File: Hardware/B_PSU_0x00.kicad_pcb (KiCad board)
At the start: 2 copper layers, 111.8 x 73.7 mm, 103 parts, among them J1 Conn_01x03, J10 Conn_01x02, J11 Conn_01x02, J12 Conn_01x02, J13 Conn_01x02, J14 Conn_01x02, J15 Conn_01x02, J16 Conn_01x03, J17 Conn_01x02, J2 Conn_01x02, J3 Conn_01x02, J4 Conn_01x02, J5 Conn_01x02, J6 Conn_01x02, J7 Conn_01x03, J8 Conn_01x02, J9 Conn_01x03, U1 ADP5070AREZ, U2 ADP7142AUJZ, U3 ADP7182AUJZ, U5 ADP7142AUJZ, U7 ADP7182AUJZ, U8 ADP5070AREZ

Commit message: Update B_PSU_0x00.kicad_pcb
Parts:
- removed COUT3, COUT4: 10uF, Capacitor_SMD:C_1210_3225Metric_Pad1.33x2.70mm_HandSolder
- removed Cc3: 68nF, Capacitor_SMD:C_0805_2012Metric_Pad1.18x1.45mm_HandSolder
- removed Cc4: 47nF, Capacitor_SMD:C_0805_2012Metric_Pad1.18x1.45mm_HandSolder
- removed Cin2: 10uF, Capacitor_SMD:C_1206_3216Metric_Pad1.33x1.80mm_HandSolder
- removed Cvref2, Cvreg2: 1uF, Capacitor_SMD:C_0805_2012Metric_Pad1.18x1.45mm_HandSolder
- removed D10, D3: DFLS240, Diode_SMD:D_SOD-123F
- removed J11, J12, J17, J4, J6: Conn_01x02, Connector_PinHeader_2.54mm:PinHeader_1x02_P2.54mm_Vertical
- removed J15: Conn_01x02, TerminalBlock:TerminalBlock_bornier-2_P5.08mm
- removed J16: Conn_01x03, TerminalBlock:TerminalBlock_bornier-3_P5.08mm
- removed L3: 15uH, Inductor_SMD:L_Coilcraft_XxL4030
- removed L4: 6.8uH, Inductor_SMD:L_Coilcraft_XxL4040
- removed Rc3: 15k, Resistor_SMD:R_0805_2012Metric_Pad1.20x1.40mm_HandSolder
- removed Rc4: 12k, Resistor_SMD:R_0805_2012Metric_Pad1.20x1.40mm_HandSolder
- removed Rfb10, Rfb9: 113k, Resistor_SMD:R_0805_2012Metric_Pad1.20x1.40mm_HandSolder
- removed Rft10, Rft9: 2.15M, Resistor_SMD:R_0805_2012Metric_Pad1.20x1.40mm_HandSolder
- removed U8: ADP5070AREZ, Package_SO:ETSSOP-20-1EP_4.4x6.5mm_P0.65mm_EP3x4.2mm

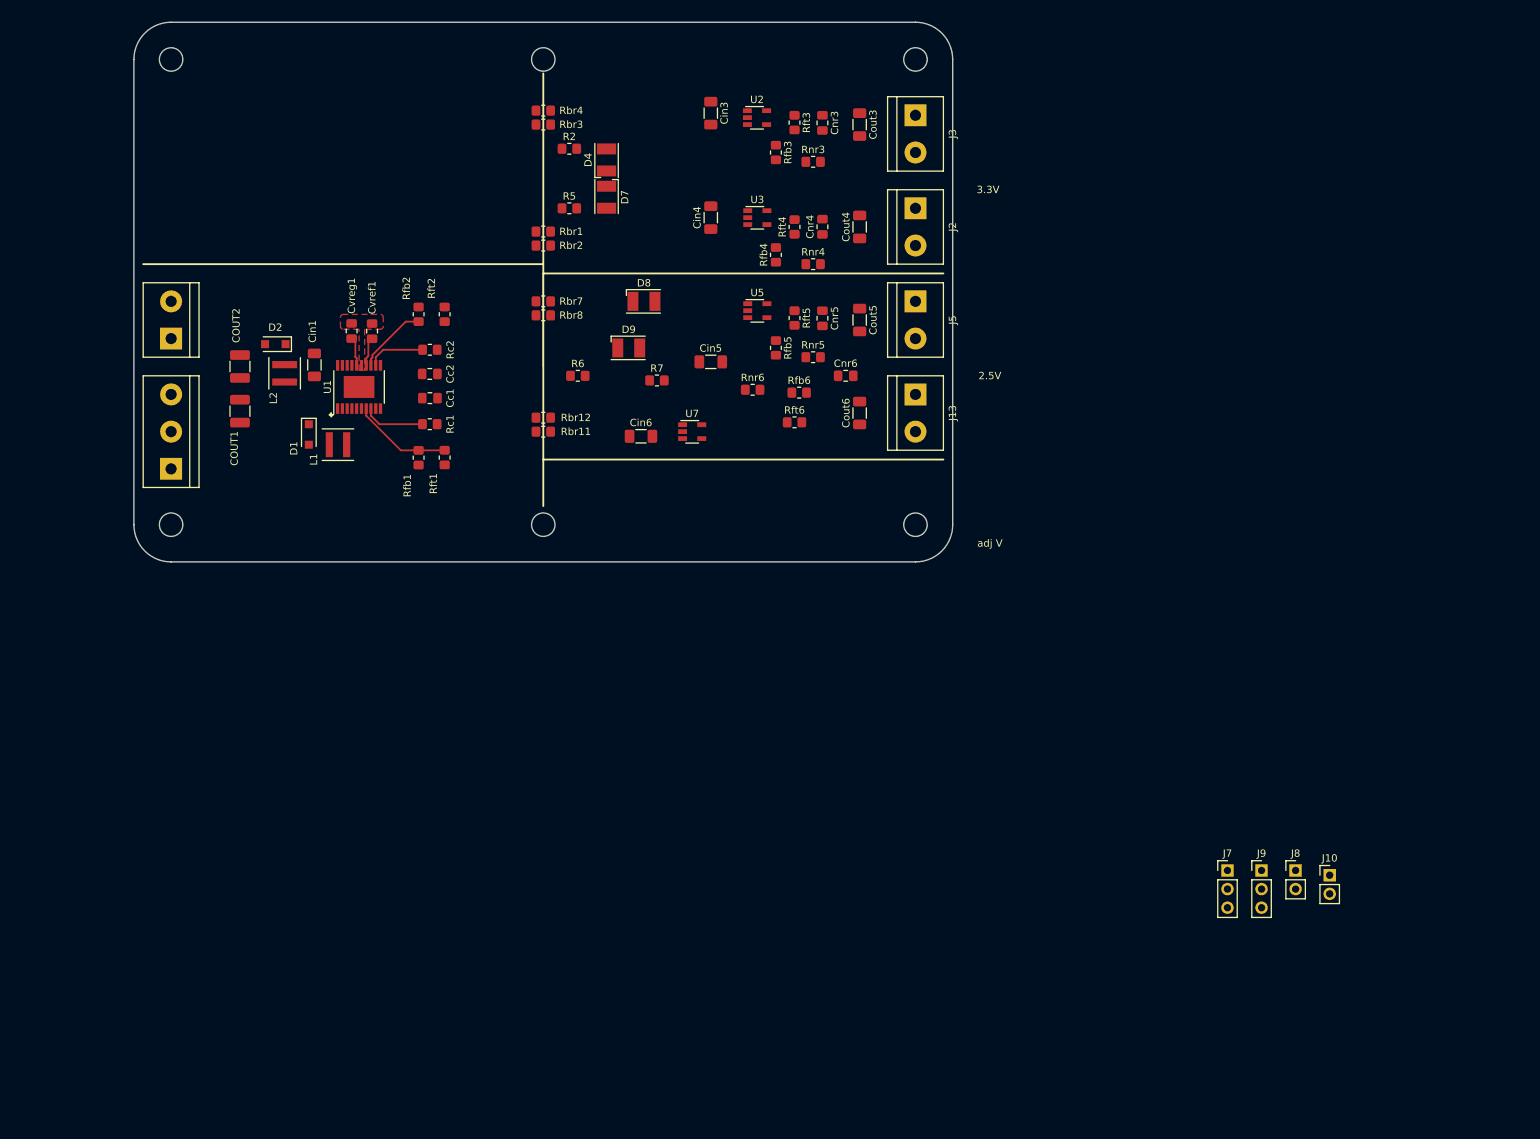
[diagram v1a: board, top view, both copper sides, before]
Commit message: LDO's changed to the ones you can buy
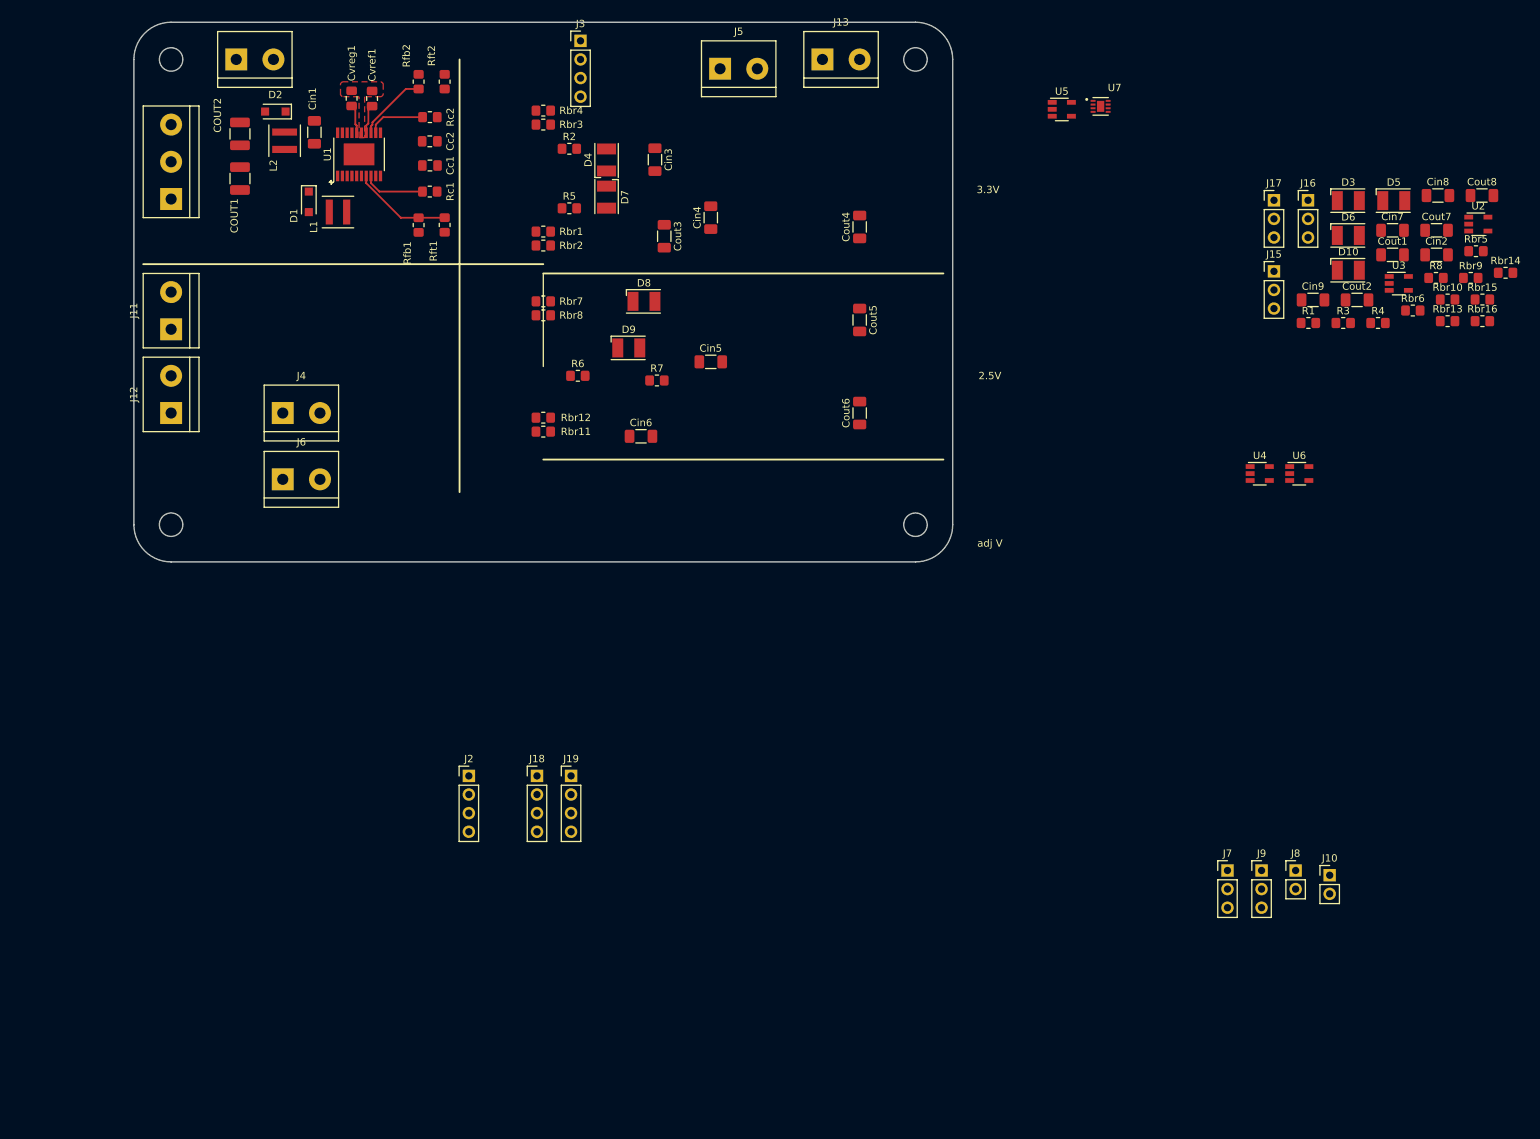
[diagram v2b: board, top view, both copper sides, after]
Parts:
- removed Cnr3, Cnr4, Cnr5, Cnr6: 1uF, Capacitor_SMD:C_0805_2012Metric_Pad1.18x1.45mm_HandSolder
- removed H3, H6: MountingHole, MountingHole:MountingHole_3.2mm_M3
- removed Rfb3, Rfb4, Rfb5, Rfb6: 10k, Resistor_SMD:R_0805_2012Metric_Pad1.20x1.40mm_HandSolder
- removed Rft3, Rft4, Rft5, Rft6: 20k, Resistor_SMD:R_0805_2012Metric_Pad1.20x1.40mm_HandSolder
- removed Rnr3, Rnr4, Rnr5, Rnr6: 1k, Resistor_SMD:R_0805_2012Metric_Pad1.20x1.40mm_HandSolder
- added Cin2: 10uF, Capacitor_SMD:C_1206_3216Metric_Pad1.33x1.80mm_HandSolder, F.Cu at (213.4, 47.0)
- added Cin7: 10uF, Capacitor_SMD:C_1206_3216Metric_Pad1.33x1.80mm_HandSolder, F.Cu at (207.3, 43.6)
- added Cin8: 10uF, Capacitor_SMD:C_1206_3216Metric_Pad1.33x1.80mm_HandSolder, F.Cu at (213.6, 38.9)
- added Cin9: 10uF, Capacitor_SMD:C_1206_3216Metric_Pad1.33x1.80mm_HandSolder, F.Cu at (196.5, 53.1)
- added Cout1: 2.2uF, Capacitor_SMD:C_1206_3216Metric_Pad1.33x1.80mm_HandSolder, F.Cu at (207.3, 47.0)
- added Cout2: 2.2uF, Capacitor_SMD:C_1206_3216Metric_Pad1.33x1.80mm_HandSolder, F.Cu at (202.5, 53.1)
- added Cout7: 2.2uF, Capacitor_SMD:C_1206_3216Metric_Pad1.33x1.80mm_HandSolder, F.Cu at (213.4, 43.6)
- added Cout8: 2.2uF, Capacitor_SMD:C_1206_3216Metric_Pad1.33x1.80mm_HandSolder, F.Cu at (219.6, 38.9)
- added D10: LED, LED_SMD:LED_PLCC-2, F.Cu at (201.3, 49.1)
- added D3: LED, LED_SMD:LED_PLCC-2, F.Cu at (201.3, 39.6)
- added D5: LED, LED_SMD:LED_PLCC-2, F.Cu at (207.5, 39.6)
- added D6: LED, LED_SMD:LED_PLCC-2, F.Cu at (201.3, 44.3)
- added J11: Conn_01x02, TerminalBlock:TerminalBlock_bornier-2_P5.08mm, F.Cu at (40.6, 57.1)
- added J12: Conn_01x02, TerminalBlock:TerminalBlock_bornier-2_P5.08mm, F.Cu at (40.6, 68.6)
- added J15: Conn_01x03, Connector_PinHeader_2.54mm:PinHeader_1x03_P2.54mm_Vertical, F.Cu at (191.2, 49.2)
- added J16: Conn_01x03, Connector_PinHeader_2.54mm:PinHeader_1x03_P2.54mm_Vertical, F.Cu at (195.8, 39.5)
- added J17: Conn_01x03, Connector_PinHeader_2.54mm:PinHeader_1x03_P2.54mm_Vertical, F.Cu at (191.2, 39.5)
- added J18: Conn_01x04, Connector_PinHeader_2.54mm:PinHeader_1x04_P2.54mm_Vertical, F.Cu at (90.6, 118.1)
- added J19: Conn_01x04, Connector_PinHeader_2.54mm:PinHeader_1x04_P2.54mm_Vertical, F.Cu at (95.2, 118.1)
- added J4: Conn_01x02, TerminalBlock:TerminalBlock_bornier-2_P5.08mm, F.Cu at (55.9, 68.6)
- added J6: Conn_01x02, TerminalBlock:TerminalBlock_bornier-2_P5.08mm, F.Cu at (55.9, 77.6)
- added R1: 0R, Resistor_SMD:R_0805_2012Metric_Pad1.20x1.40mm_HandSolder, F.Cu at (195.9, 56.3)
- added R3: 0R, Resistor_SMD:R_0805_2012Metric_Pad1.20x1.40mm_HandSolder, F.Cu at (200.6, 56.3)
- added R4: 0R, Resistor_SMD:R_0805_2012Metric_Pad1.20x1.40mm_HandSolder, F.Cu at (205.4, 56.3)
- added R8: 0R, Resistor_SMD:R_0805_2012Metric_Pad1.20x1.40mm_HandSolder, F.Cu at (213.3, 50.1)
- added Rbr10: 0R, Resistor_SMD:R_0805_2012Metric_Pad1.20x1.40mm_HandSolder, F.Cu at (214.9, 53.1)
- added Rbr13: 0R, Resistor_SMD:R_0805_2012Metric_Pad1.20x1.40mm_HandSolder, F.Cu at (214.9, 56.0)
- added Rbr14: 0R, Resistor_SMD:R_0805_2012Metric_Pad1.20x1.40mm_HandSolder, F.Cu at (222.8, 49.4)
- added Rbr15: 0R, Resistor_SMD:R_0805_2012Metric_Pad1.20x1.40mm_HandSolder, F.Cu at (219.6, 53.1)
- added Rbr16: 0R, Resistor_SMD:R_0805_2012Metric_Pad1.20x1.40mm_HandSolder, F.Cu at (219.6, 56.0)
- added Rbr5: 0R, Resistor_SMD:R_0805_2012Metric_Pad1.20x1.40mm_HandSolder, F.Cu at (218.7, 46.5)
- added Rbr6: 0R, Resistor_SMD:R_0805_2012Metric_Pad1.20x1.40mm_HandSolder, F.Cu at (210.1, 54.6)
- added Rbr9: 0R, Resistor_SMD:R_0805_2012Metric_Pad1.20x1.40mm_HandSolder, F.Cu at (218.0, 50.1)
- added U4: ADP7142AUJZ-1.8, Package_TO_SOT_SMD:TSOT-23-5, F.Cu at (189.2, 76.8)
- added U6: ADP7142AUJZ-2.5, Package_TO_SOT_SMD:TSOT-23-5, F.Cu at (194.6, 76.8)
- J2, J3: value Conn_01x02 -> Conn_01x04; footprint TerminalBlock:TerminalBlock_bornier-2_P5.08mm -> Connector_PinHeader_2.54mm:PinHeader_1x04_P2.54mm_Vertical
- U2: value ADP7142AUJZ -> ADP7142AUJZ-5.0
- U3: value ADP7182AUJZ -> ADP7142AUJZ-3.3
- U5: value ADP7142AUJZ -> ADP7182AUJZ-1.8
- U7: value ADP7182AUJZ -> ADP7183ACPZN3.3-R7; footprint Package_TO_SOT_SMD:TSOT-23-5 -> SAE_spec:SON50P200X200X60-9N
- moved U2 99.5 mm to (219.1, 42.8)
- moved J2 98.6 mm to (81.3, 118.1), turned to 0 degrees
- moved U3 88.0 mm to (208.2, 50.9)
- moved U7 71.3 mm to (167.5, 26.7)
- moved U5 49.8 mm to (162.2, 27.1)
- moved J13 47.5 mm to (129.5, 20.3), turned to 0 degrees
- moved J3 46.8 mm to (96.5, 17.8), turned to 0 degrees
- moved J5 41.5 mm to (115.6, 21.6), turned to 0 degrees
- moved J14 39.1 mm to (49.5, 20.3), turned to 0 degrees
- moved J1 36.8 mm to (40.6, 39.4)
- moved D1 31.8 mm to (59.4, 39.8)
- moved Cc2 31.8 mm to (75.9, 31.5)
- moved Cvref1 31.8 mm to (68.1, 25.7)
- moved D2 31.8 mm to (54.9, 27.4)
- moved Rc2 31.8 mm to (76.0, 28.2)
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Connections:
- Cout3 pad 1: Net-(Cnr3-Pad1) -> Net-(Cout3-Pad1)
- Cout4 pad 2: Net-(Cnr4-Pad2) -> Net-(Cout4-Pad2)
- Cout5 pad 1: Net-(Cnr5-Pad1) -> Net-(Cout5-Pad1)
- Cout6 pad 2: Net-(Cnr6-Pad2) -> Net-(Cout6-Pad2)
- J13 pad 1: Net-(Cnr6-Pad2) -> Net-(Cout6-Pad2)
- J2 pad 1: Net-(Cnr4-Pad2) -> (no net)
- J2 pad 2: GNDA -> (no net)
- J3 pad 1: Net-(Cnr3-Pad1) -> Net-(Cout3-Pad1)
- J5 pad 1: Net-(Cnr5-Pad1) -> Net-(Cout5-Pad1)
- J9 pad 1: (no net) -> Net-(Cin3-Pad1)
- J9 pad 2: (no net) -> Net-(J9-Pad2)
- J9 pad 3: (no net) -> GNDA
- U2 pad 1: Net-(Cin3-Pad1) -> Net-(Cin2-Pad1)
- U2 pad 3: (no net) -> Net-(J15-Pad2)
- U2 pad 4: Net-(Rfb3-Pad1) -> (no net)
- U2 pad 5: Net-(Cnr3-Pad1) -> Net-(Cout2-Pad1)
- U3 pad 1: GNDA -> Net-(Cin3-Pad1)
- U3 pad 2: Net-(Cin4-Pad1) -> GNDA
- U3 pad 3: (no net) -> Net-(J9-Pad2)
- U3 pad 4: Net-(Rfb4-Pad2) -> Net-(Cout3-Pad1)
- U3 pad 5: Net-(Cnr4-Pad2) -> Net-(Cout3-Pad1)
- U5 pad 1: Net-(Cin5-Pad1) -> (no net)
- U5 pad 2: GNDA -> (no net)
- U5 pad 4: Net-(Rfb5-Pad1) -> (no net)
- U5 pad 5: Net-(Cnr5-Pad1) -> (no net)
- U7 pad 1: GNDA -> (no net)
- U7 pad 2: Net-(Cin6-Pad1) -> (no net)
- U7 pad 4: Net-(Rfb6-Pad2) -> (no net)
- U7 pad 5: Net-(Cnr6-Pad2) -> (no net)
